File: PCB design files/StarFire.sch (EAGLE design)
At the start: 29 parts, among them U2 ATTINY85-20SU

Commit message: cleanup and sort
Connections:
- net N$13: now also U$1.+1
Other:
- note added: "Atmel ATTiny85 MCU"
- note added: "Battery and switch"
- note added: "Charlieplexed LED array"
- moved on the sheet: C1, C2, LED1, LED10, LED11, LED12, LED2, LED3, LED4, LED5, LED6, LED7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

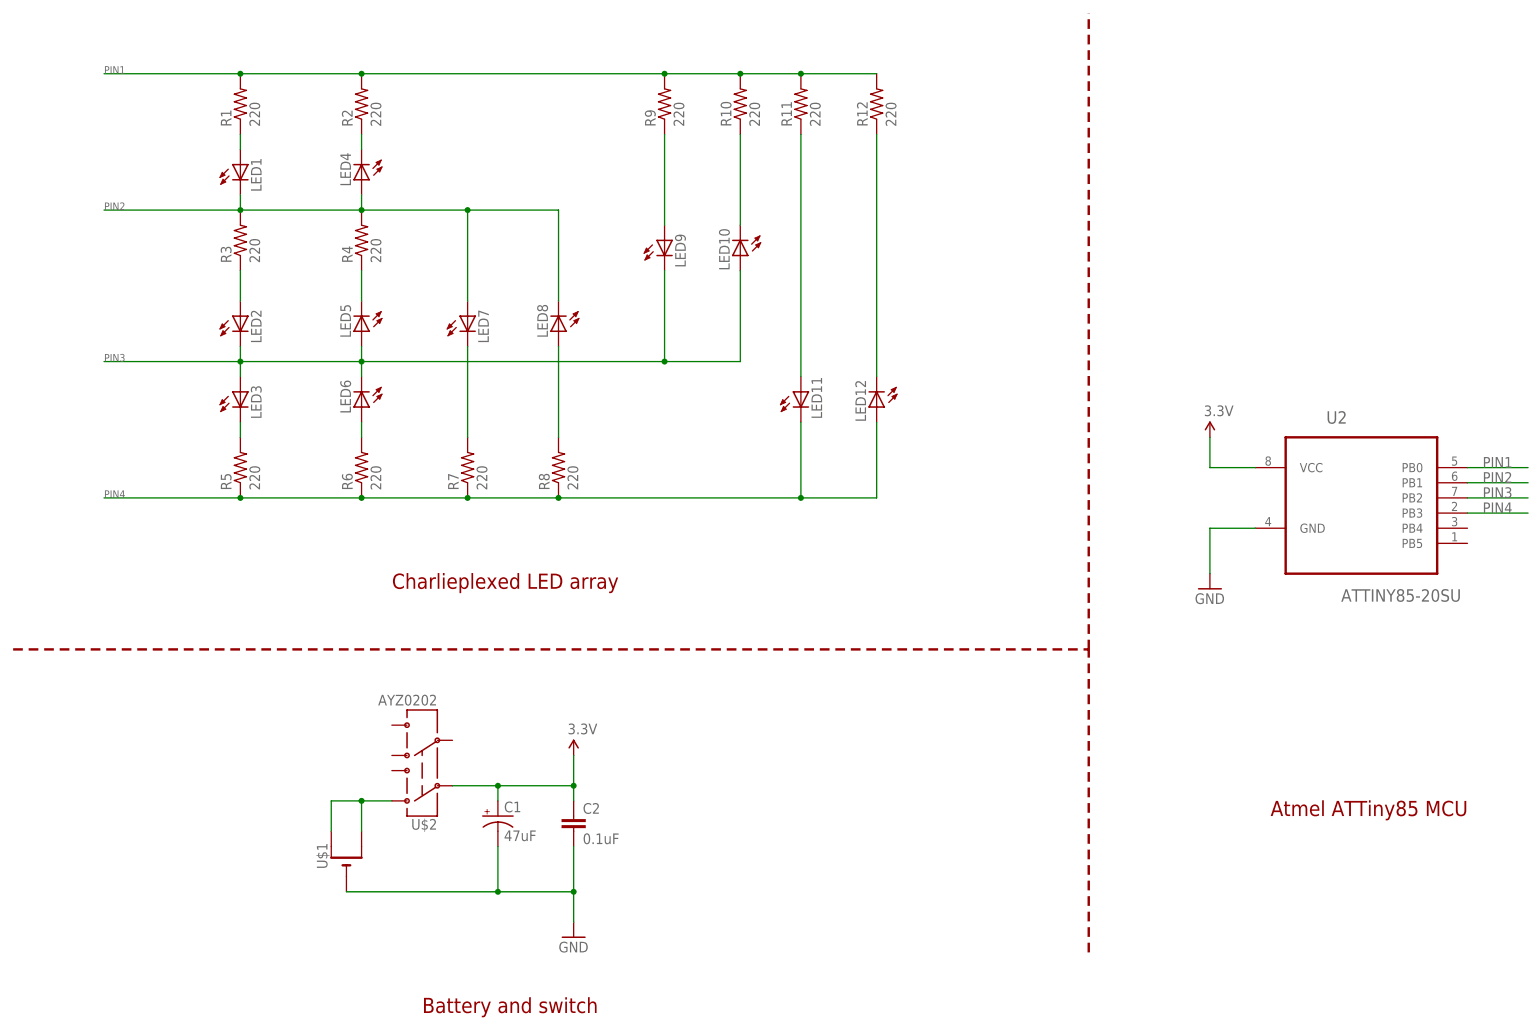
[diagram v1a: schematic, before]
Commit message: Fixed routing errors
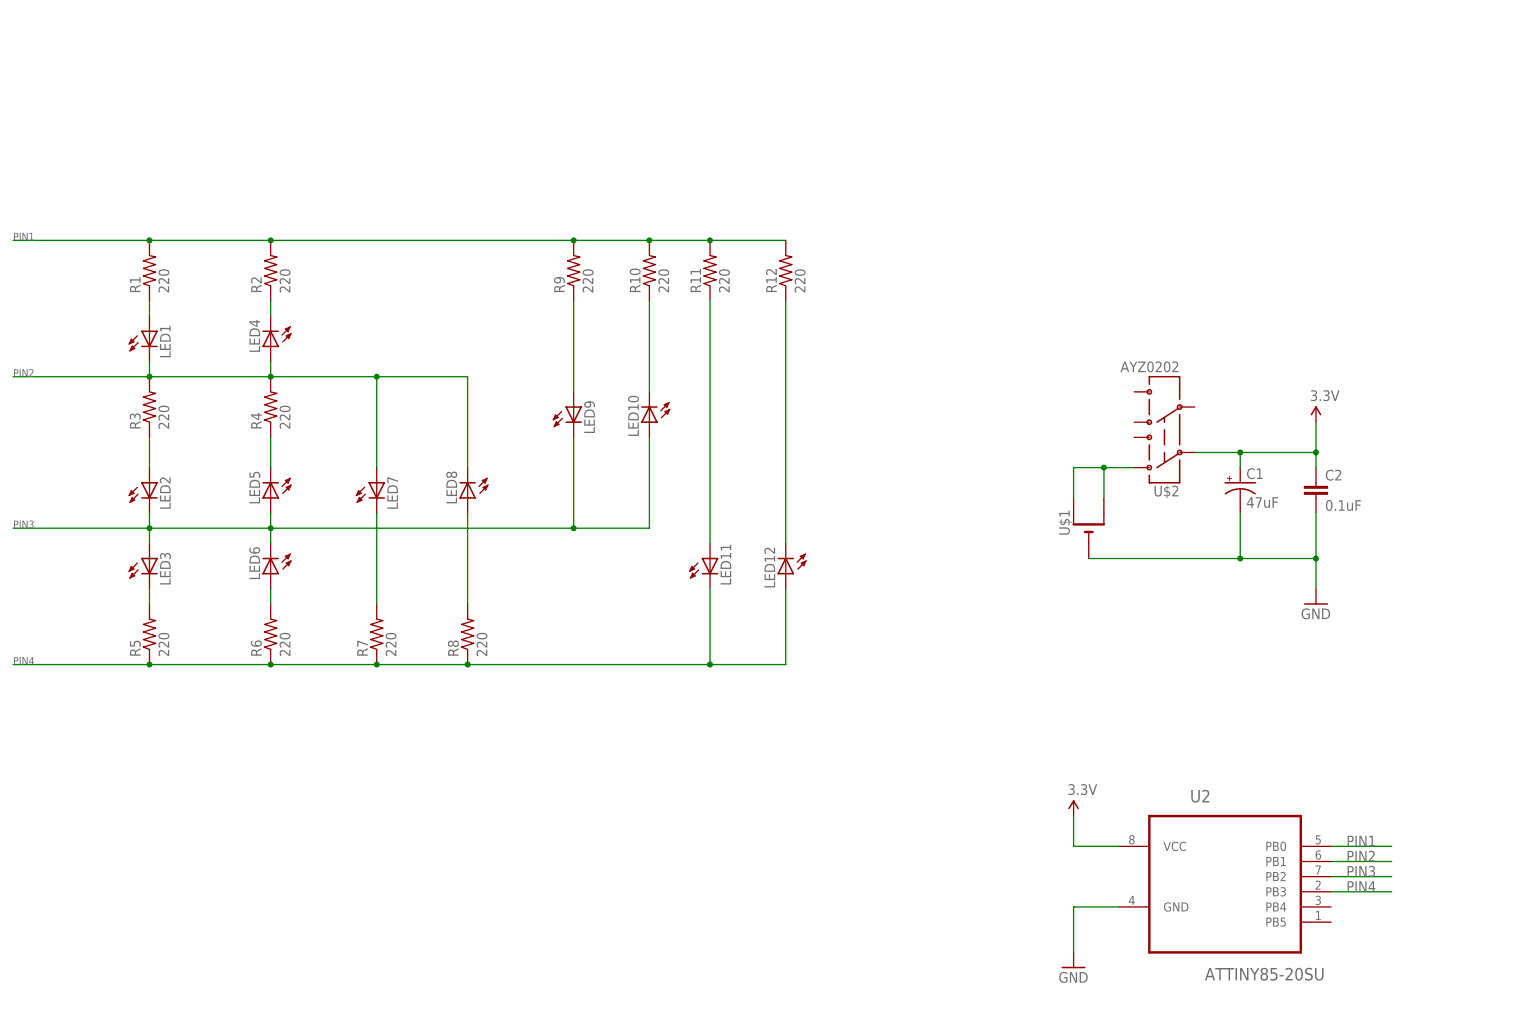
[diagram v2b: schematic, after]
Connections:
- net N$13: no longer U$1.+1
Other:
- note removed: "Atmel ATTiny85 MCU"
- note removed: "Battery and switch"
- note removed: "Charlieplexed LED array"
- moved on the sheet: C1, C2, LED1, LED10, LED11, LED12, LED2, LED3, LED4, LED5, LED6, LED7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
